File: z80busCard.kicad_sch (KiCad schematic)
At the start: 4 parts, among them J1 Conn_02x20_Odd_Even, J2 Conn_02x20_Odd_Even, J3 Conn_02x20_Odd_Even, J4 Conn_02x20_Odd_Even

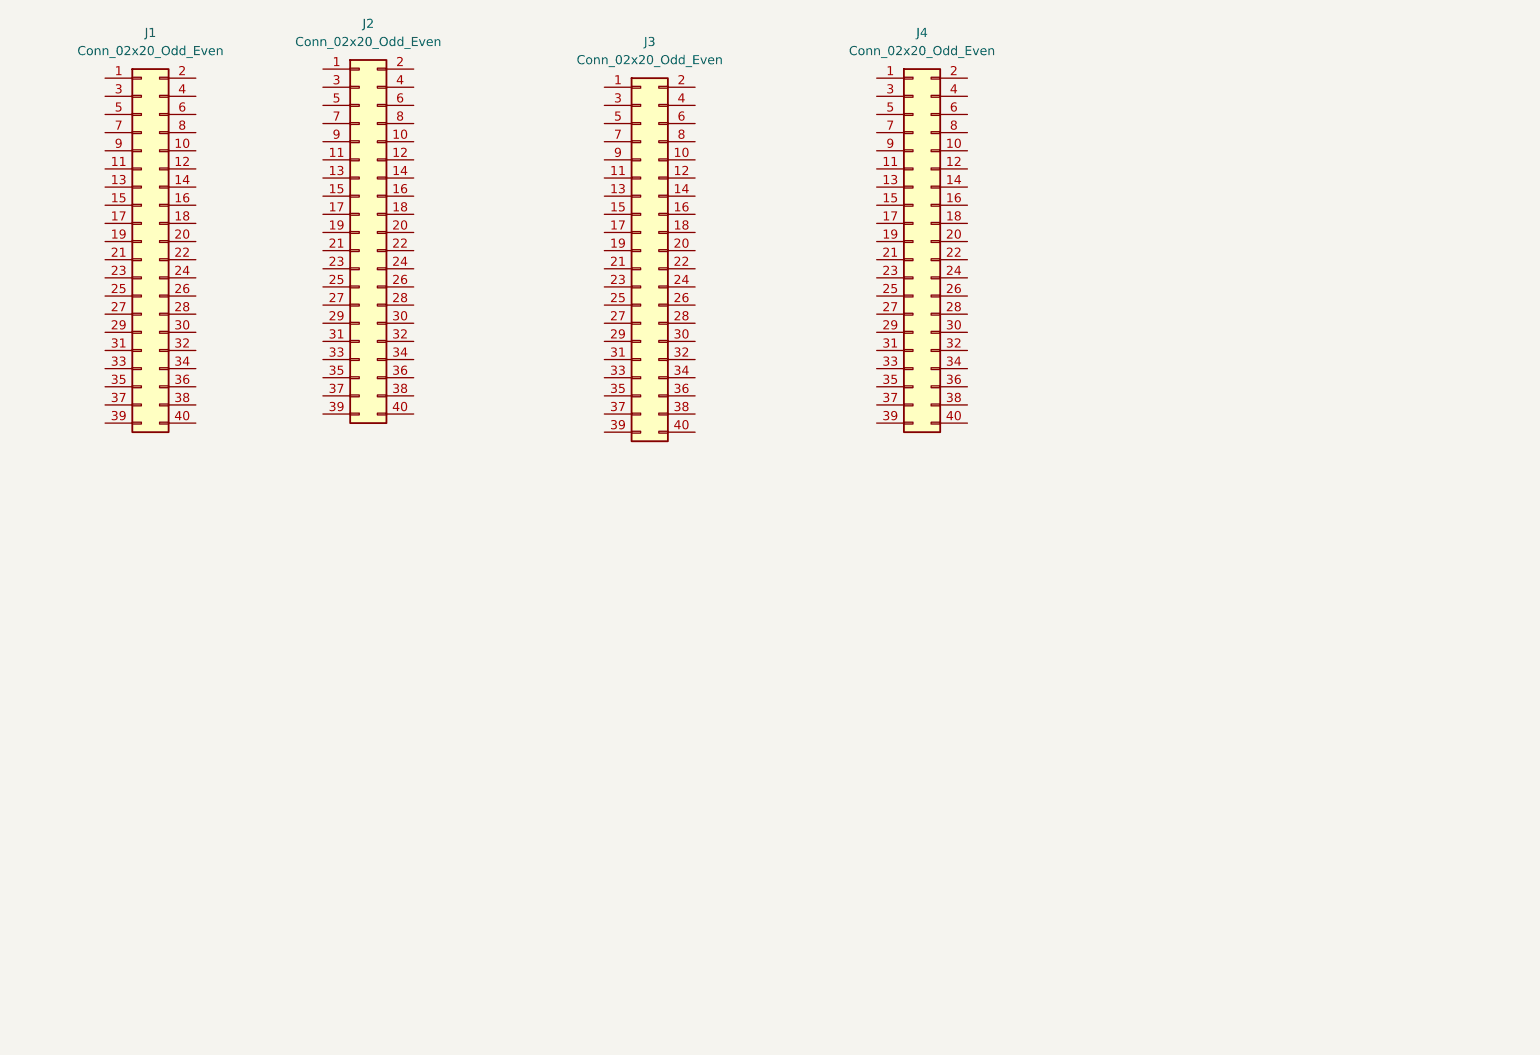
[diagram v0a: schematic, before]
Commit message: Added reset circuit
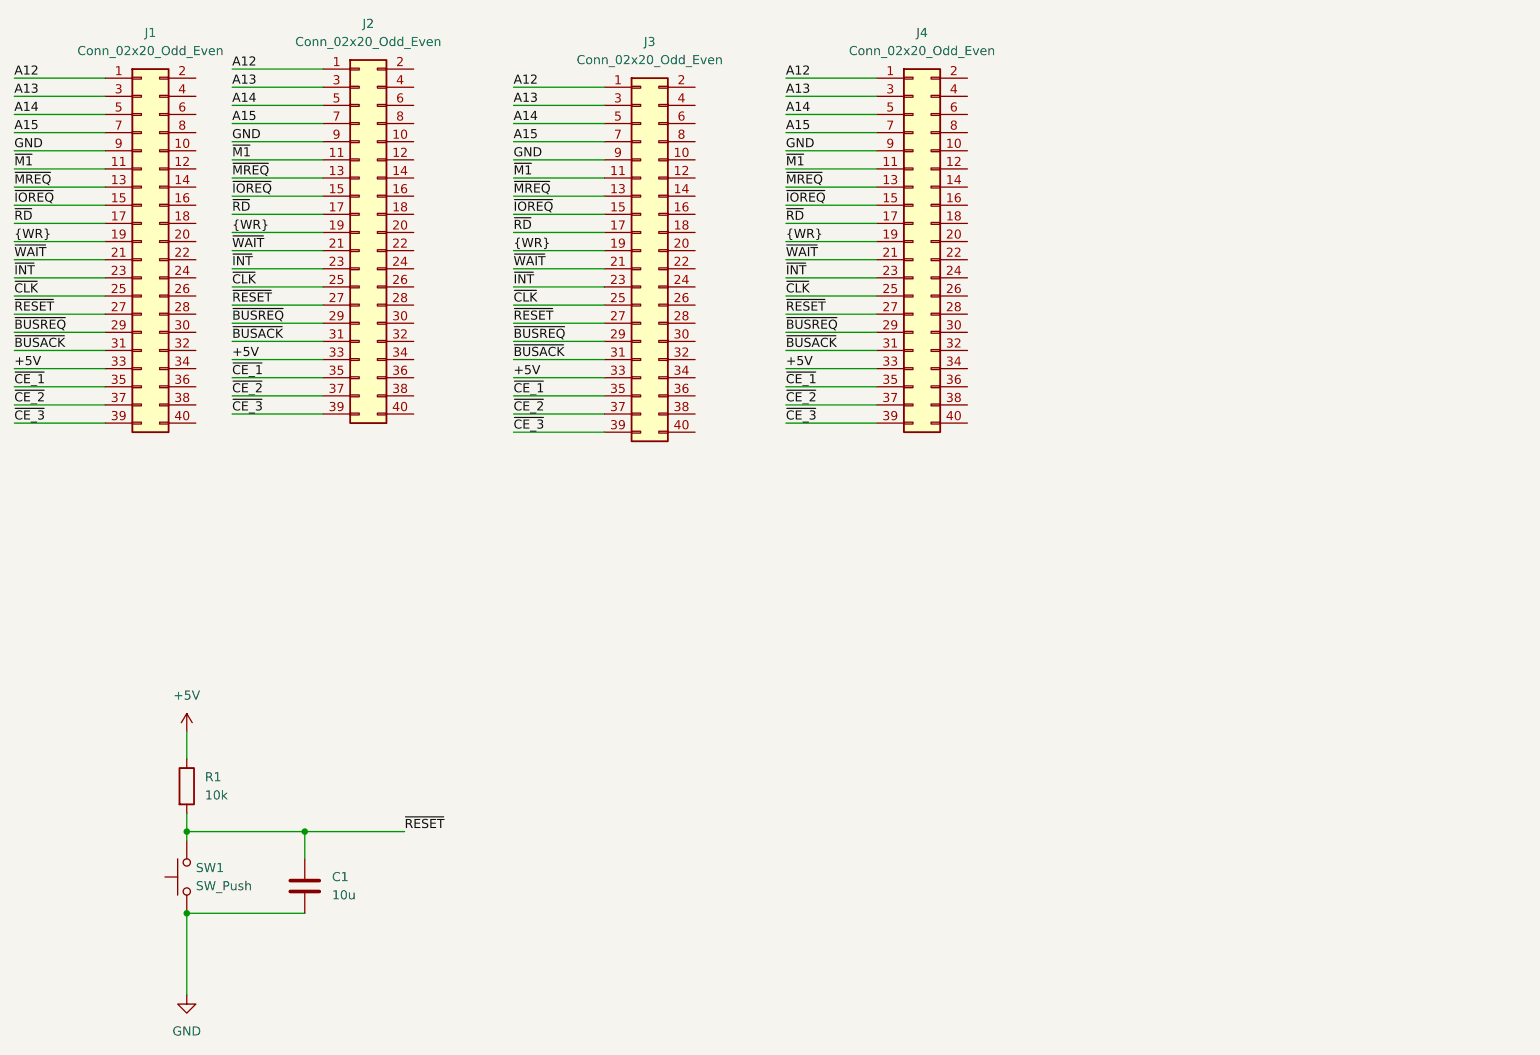
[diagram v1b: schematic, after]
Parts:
- added C1: 10u, symbol Device:C
- added R1: 10k, symbol Device:R
- added SW1: SW_Push, Button_Switch_THT:SW_PUSH_6mm_H4.3mm, symbol Switch:SW_Push
- J1, J2, J3: footprint Connector_PinSocket_2.54mm:PinSocket_2x20_P2.54mm_Vertical -> Library:PinSocket_2x20_P2.54mm_Vertical_Mirrored
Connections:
- net A12: now reaches J3.1 (Pin_1)
- net A12: now also J1.1 (Pin_1), J2.1 (Pin_1), J4.1 (Pin_1)
- net ~{M1}: now reaches J3.11 (Pin_11)
- net ~{M1}: now also J1.11 (Pin_11), J2.11 (Pin_11), J4.11 (Pin_11)
- net ~{MREQ}: now reaches J3.13 (Pin_13)
- net ~{MREQ}: now also J1.13 (Pin_13), J2.13 (Pin_13), J4.13 (Pin_13)
- net ~{IOREQ}: now reaches J3.15 (Pin_15)
- net ~{IOREQ}: now also J1.15 (Pin_15), J2.15 (Pin_15), J4.15 (Pin_15)
- net ~{RD}: now reaches J3.17 (Pin_17)
- net ~{RD}: now also J1.17 (Pin_17), J2.17 (Pin_17), J4.17 (Pin_17)
- net {WR}: now reaches J3.19 (Pin_19)
- net {WR}: now also J1.19 (Pin_19), J2.19 (Pin_19), J4.19 (Pin_19)
- net ~{WAIT}: now reaches J3.21 (Pin_21)
- net ~{WAIT}: now also J1.21 (Pin_21), J2.21 (Pin_21), J4.21 (Pin_21)
- net ~{INT}: now reaches J3.23 (Pin_23)
- net ~{INT}: now also J1.23 (Pin_23), J2.23 (Pin_23), J4.23 (Pin_23)
- net ~{CLK}: now reaches J3.25 (Pin_25)
- net ~{CLK}: now also J1.25 (Pin_25), J2.25 (Pin_25), J4.25 (Pin_25)
- net ~{RESET}: now reaches J3.27 (Pin_27)
- net ~{RESET}: now also J1.27 (Pin_27), J2.27 (Pin_27), J4.27 (Pin_27), C1.1, R1.2, SW1.2
- net ~{BUSREQ}: now reaches J3.29 (Pin_29)
- net ~{BUSREQ}: now also J1.29 (Pin_29), J2.29 (Pin_29), J4.29 (Pin_29)
- net A13: now reaches J3.3 (Pin_3)
- net A13: now also J1.3 (Pin_3), J2.3 (Pin_3), J4.3 (Pin_3)
- net ~{BUSACK}: now reaches J3.31 (Pin_31)
- net ~{BUSACK}: now also J1.31 (Pin_31), J2.31 (Pin_31), J4.31 (Pin_31)
- net +5V: now reaches J3.33 (Pin_33)
- net +5V: now also J1.33 (Pin_33), J2.33 (Pin_33), J4.33 (Pin_33), R1.1
- net ~{CE_1}: now reaches J3.35 (Pin_35)
- net ~{CE_1}: now also J1.35 (Pin_35), J2.35 (Pin_35), J4.35 (Pin_35)
- net ~{CE_2}: now reaches J3.37 (Pin_37)
- net ~{CE_2}: now also J1.37 (Pin_37), J2.37 (Pin_37), J4.37 (Pin_37)
- net ~{CE_3}: now reaches J3.39 (Pin_39)
- net ~{CE_3}: now also J1.39 (Pin_39), J2.39 (Pin_39), J4.39 (Pin_39)
- net A14: now reaches J3.5 (Pin_5)
- net A14: now also J1.5 (Pin_5), J2.5 (Pin_5), J4.5 (Pin_5)
- net A15: now reaches J3.7 (Pin_7)
- net A15: now also J1.7 (Pin_7), J2.7 (Pin_7), J4.7 (Pin_7)
- net GND: now reaches J3.9 (Pin_9)
- net GND: now also J1.9 (Pin_9), J2.9 (Pin_9), J4.9 (Pin_9), C1.2, SW1.1

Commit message: Resistor footprint
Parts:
- R1: footprint (none) -> Resistor_SMD:R_0805_2012Metric_Pad1.20x1.40mm_HandSolder
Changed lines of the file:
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@@
 			)
 		)
-		(property "Footprint" ""
+		(property "Footprint" "Resistor_SMD:R_0805_2012Metric_Pad1.20x1.40mm_HandSolder"
 			(at 68.072 154.94 90)
 			(effects

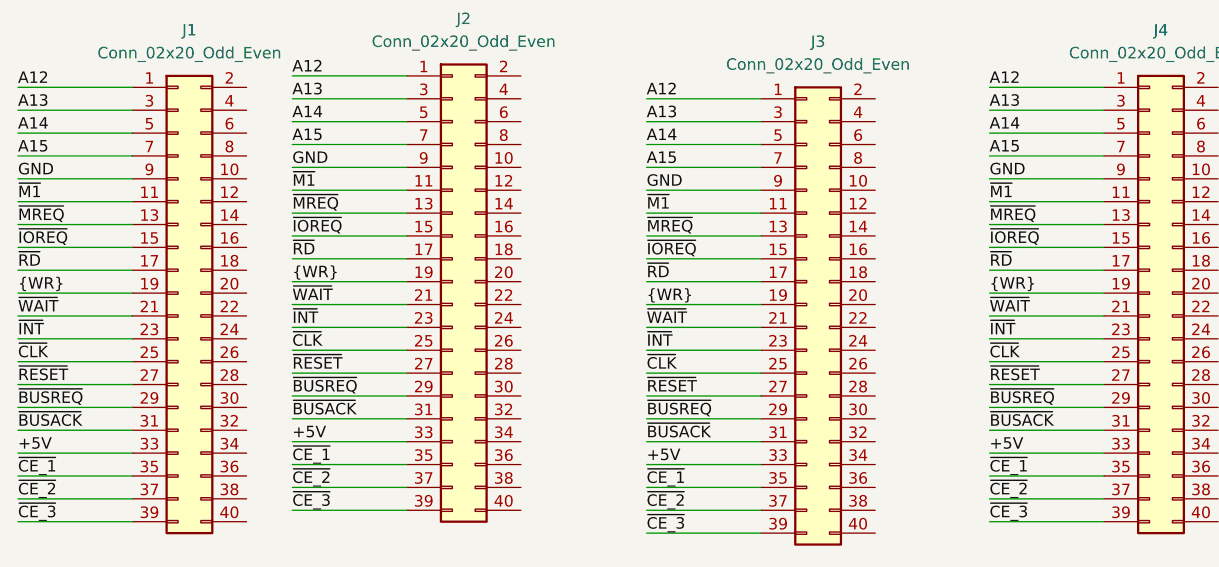
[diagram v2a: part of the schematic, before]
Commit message: Wired front layer. Added silkscreen labels
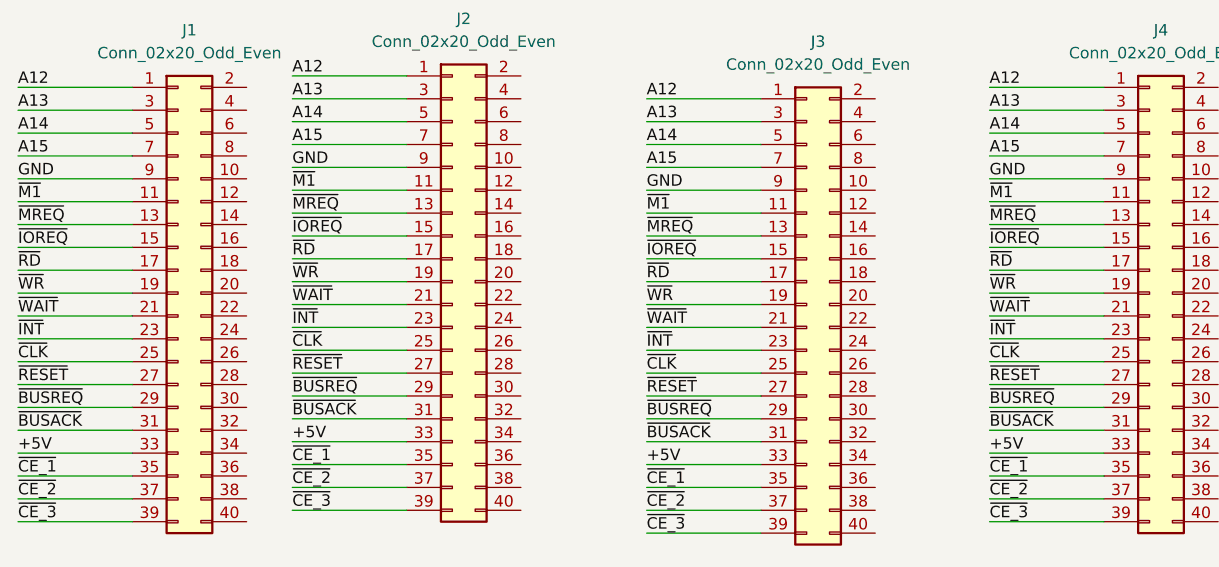
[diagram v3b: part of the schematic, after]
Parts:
- C1: footprint (none) -> Capacitor_SMD:C_0805_2012Metric_Pad1.18x1.45mm_HandSolder
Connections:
- net {WR} renamed ~{WR}
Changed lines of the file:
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@@
 		)
 	)
-	(label "{WR}"
+	(label "~{WR}"
 		(at 115.57 80.01 0)
 		(effects
@@
 		)
 	)
-	(label "{WR}"
+	(label "~{WR}"
 		(at 45.72 78.74 0)
 		(effects
@@
 		)
 	)
-	(label "{WR}"
+	(label "~{WR}"
 		(at 153.67 78.74 0)
 		(effects
@@
 		)
 	)
-	(label "{WR}"
+	(label "~{WR}"
 		(at 76.2 77.47 0)
 		(effects
@@
 			)
 		)
-		(property "Footprint" ""
+		(property "Footprint" "Capacitor_SMD:C_0805_2012Metric_Pad1.18x1.45mm_HandSolder"
 			(at 87.3252 172.72 0)
 			(effects

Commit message: Completed for order
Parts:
- added J5: USB_C_Receptacle_PowerOnly_6P, Connector_USB:USB_C_Receptacle_GCT_USB4125-xx-x_6P_TopMnt_Horizontal, symbol Connector:USB_C_Receptacle_PowerOnly_6P
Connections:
- net +5V: now also J5.A9 (VBUS), J5.B9 (VBUS)
- net GND: now also J5.A12 (GND), J5.B12 (GND), J5.S1 (SHIELD)
- net D4: now reaches J3.10 (Pin_10)
- net D4: now also J1.10 (Pin_10), J2.10 (Pin_10), J4.10 (Pin_10)
- net D5: now reaches J3.12 (Pin_12)
- net D5: now also J1.12 (Pin_12), J2.12 (Pin_12), J4.12 (Pin_12)
- net D6: now reaches J3.14 (Pin_14)
- net D6: now also J1.14 (Pin_14), J2.14 (Pin_14), J4.14 (Pin_14)
- net D7: now reaches J3.16 (Pin_16)
- net D7: now also J1.16 (Pin_16), J2.16 (Pin_16), J4.16 (Pin_16)
- net A0: now reaches J3.18 (Pin_18)
- net A0: now also J1.18 (Pin_18), J2.18 (Pin_18), J4.18 (Pin_18)
- net D0: now reaches J3.2 (Pin_2)
- net D0: now also J1.2 (Pin_2), J2.2 (Pin_2), J4.2 (Pin_2)
- net A1: now reaches J3.20 (Pin_20)
- net A1: now also J1.20 (Pin_20), J2.20 (Pin_20), J4.20 (Pin_20)
- net A2: now reaches J3.22 (Pin_22)
- net A2: now also J1.22 (Pin_22), J2.22 (Pin_22), J4.22 (Pin_22)
- net A3: now reaches J3.24 (Pin_24)
- net A3: now also J1.24 (Pin_24), J2.24 (Pin_24), J4.24 (Pin_24)
- net A4: now reaches J3.26 (Pin_26)
- net A4: now also J1.26 (Pin_26), J2.26 (Pin_26), J4.26 (Pin_26)
- net A5: now reaches J3.28 (Pin_28)
- net A5: now also J1.28 (Pin_28), J2.28 (Pin_28), J4.28 (Pin_28)
- net A6: now reaches J3.30 (Pin_30)
- net A6: now also J1.30 (Pin_30), J2.30 (Pin_30), J4.30 (Pin_30)
- net A7: now reaches J3.32 (Pin_32)
- net A7: now also J1.32 (Pin_32), J2.32 (Pin_32), J4.32 (Pin_32)
- net A8: now reaches J3.34 (Pin_34)
- net A8: now also J1.34 (Pin_34), J2.34 (Pin_34), J4.34 (Pin_34)
- net A9: now reaches J3.36 (Pin_36)
- net A9: now also J1.36 (Pin_36), J2.36 (Pin_36), J4.36 (Pin_36)
- net A10: now reaches J3.38 (Pin_38)
- net A10: now also J1.38 (Pin_38), J2.38 (Pin_38), J4.38 (Pin_38)
- net D1: now reaches J3.4 (Pin_4)
- net D1: now also J1.4 (Pin_4), J2.4 (Pin_4), J4.4 (Pin_4)
- net A11: now reaches J3.40 (Pin_40)
- net A11: now also J1.40 (Pin_40), J2.40 (Pin_40), J4.40 (Pin_40)
- net D2: now reaches J3.6 (Pin_6)
- net D2: now also J1.6 (Pin_6), J2.6 (Pin_6), J4.6 (Pin_6)
- net D3: now reaches J3.8 (Pin_8)
- net D3: now also J1.8 (Pin_8), J2.8 (Pin_8), J4.8 (Pin_8)
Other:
- moved on the sheet: J2, J3, J4

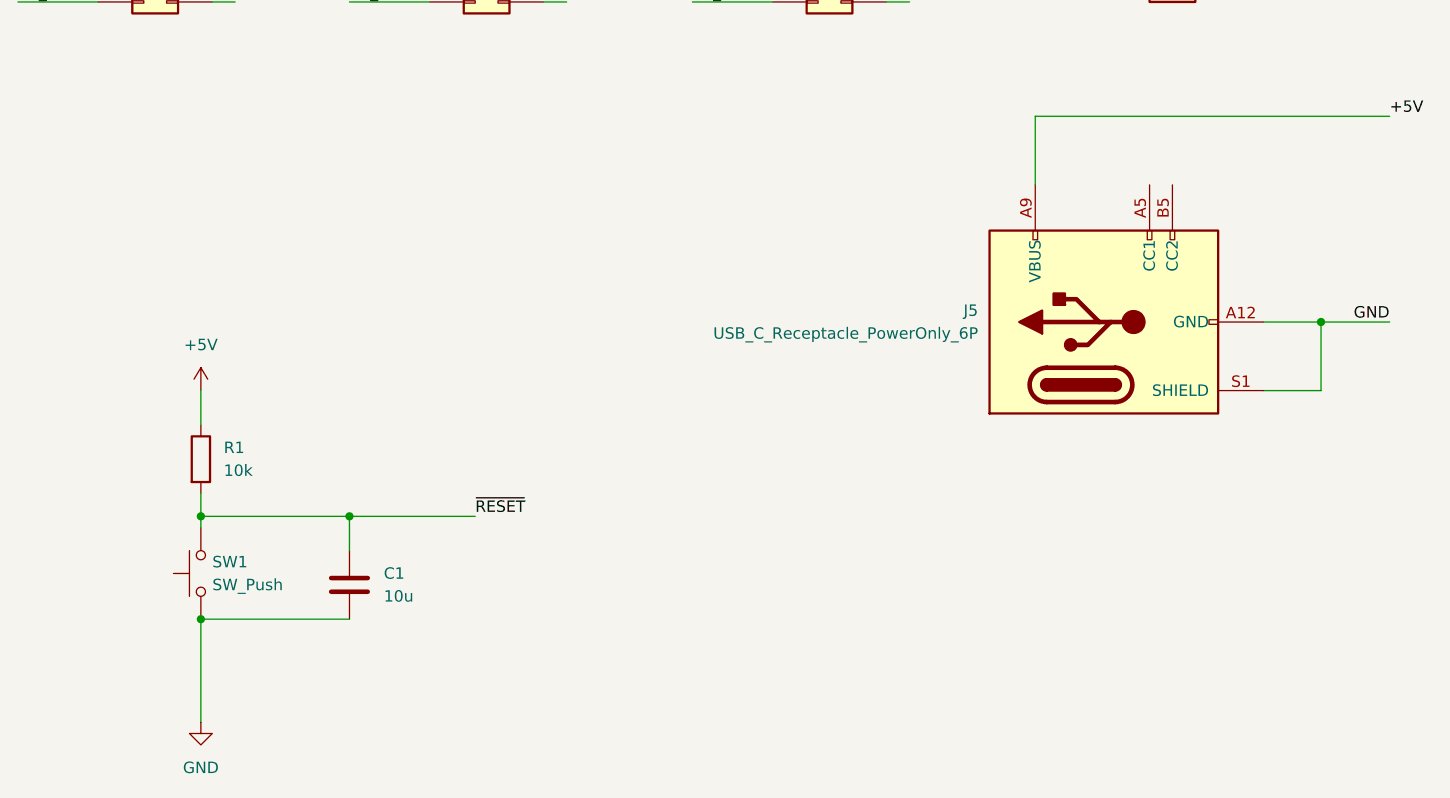
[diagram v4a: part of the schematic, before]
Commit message: Fixed USB-C power with pull-downs.  Moved connector to the side
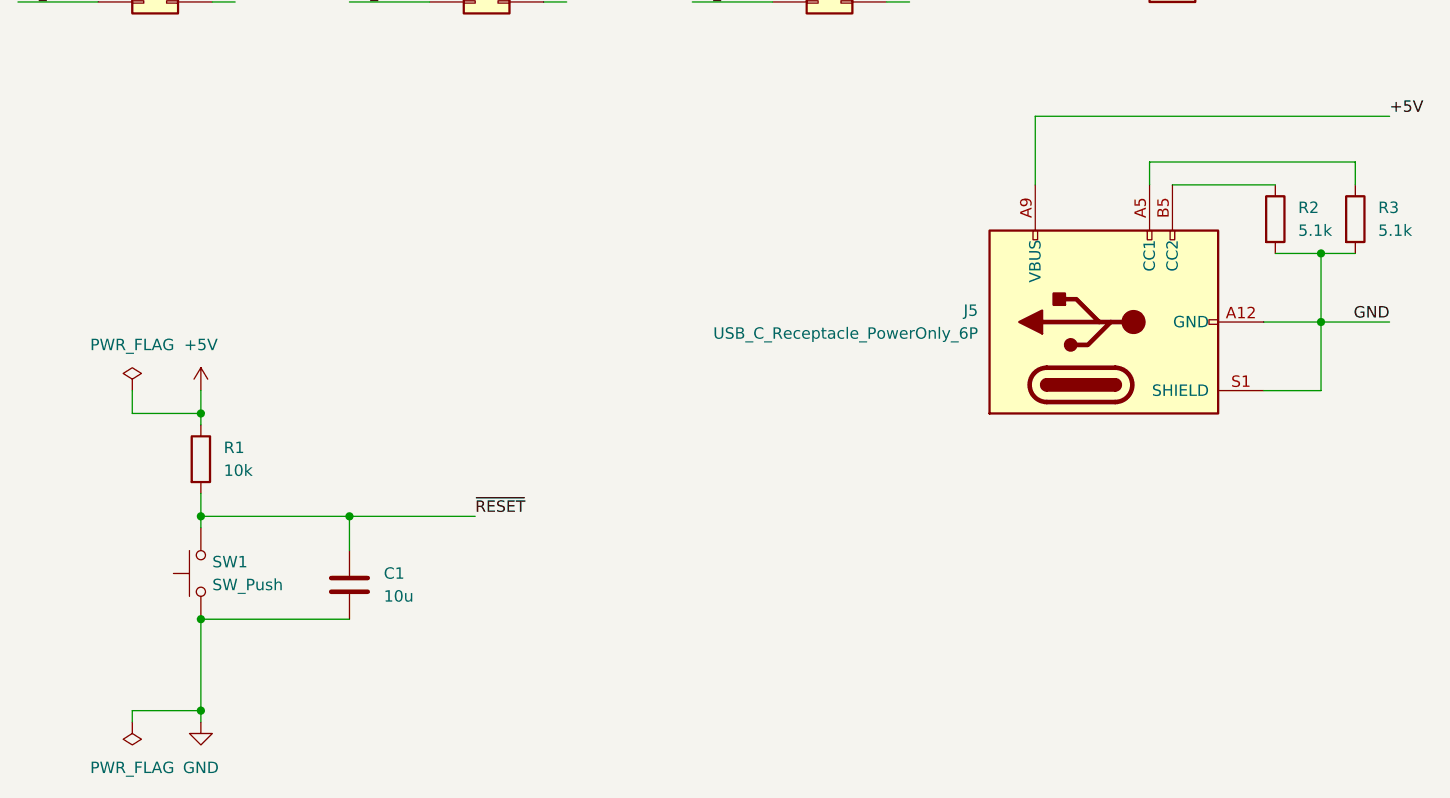
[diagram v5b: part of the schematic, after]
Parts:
- added R2, R3: 5.1k, Resistor_SMD:R_0805_2012Metric_Pad1.20x1.40mm_HandSolder, symbol Device:R
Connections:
- net GND: now also R2.2, R3.2
- net at J5.A5 (CC1): now also R3.1
- net at J5.B5 (CC2): now also R2.1
